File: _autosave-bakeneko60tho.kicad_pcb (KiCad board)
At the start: 2 copper layers, 285.8 x 95.2 mm, 160 parts, among them J1 Conn_01x04, SW1 SW_Push, U1 ATmega32U4-AU, Y1 16MHz

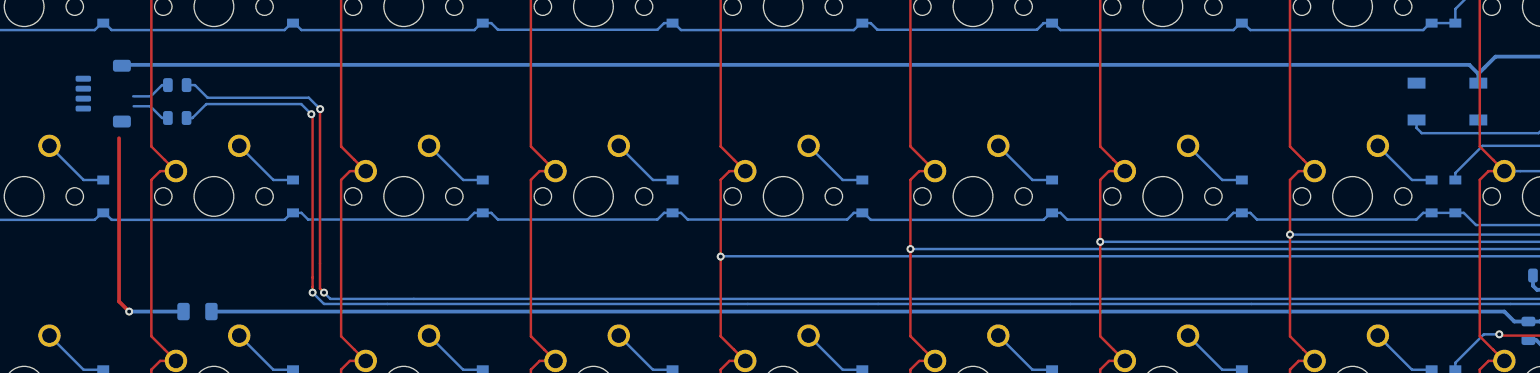
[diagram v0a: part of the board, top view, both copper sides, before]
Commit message: use jst for usb conn
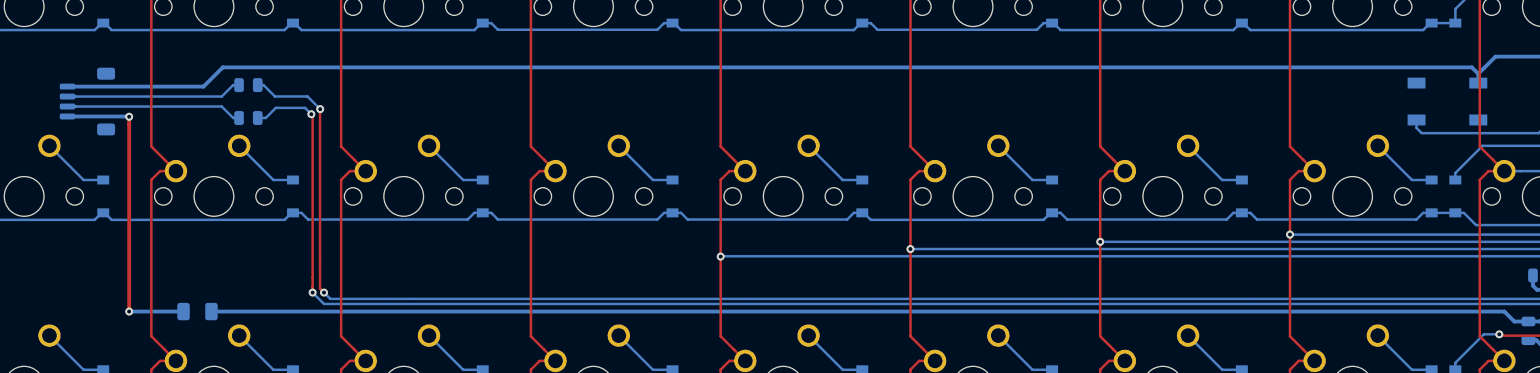
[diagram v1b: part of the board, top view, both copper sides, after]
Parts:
- moved R1 7.14 mm to (82.8, 33.4)
- moved R2 7.14 mm to (82.8, 30.1)
- moved J1 1.77 mm to (66.7, 31.8)
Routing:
- net D-: track 3.92 -> 17.7 mm
- net D+: track 3.95 -> 17.7 mm
- net VCC: track 23.3 -> 31.2 mm, vias 1 -> 2
- net Net-(R1-Pad1): track 160.2 -> 152.7 mm
- net Net-(R2-Pad1): track 160.3 -> 153.2 mm
- net GND: track 254.7 -> 260.6 mm
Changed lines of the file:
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@@
     (thickness 1.6)
     (drawings 24)
-    (tracks 1101)
+    (tracks 1107)
     (zones 0)
     (modules 160)
@@
     (visible_elements 7FFFFFFF)
     (pcbplotparams
-      (layerselection 0x010fc_ffffffff)
+      (layerselection 0x010f0_ffffffff)
       (usegerberextensions false)
       (usegerberattributes false)
@@
       (outputformat 1)
       (mirror false)
-      (drillshape 1)
+      (drillshape 0)
       (scaleselection 1)
-      (outputdirectory ""))
+      (outputdirectory "Gerbers/"))
   )
   (net 0 "")
@@
   )
   (module Connector_JST:JST_SH_SM04B-SRSS-TB_1x04-1MP_P1.00mm_Horizontal (layer B.Cu)
-    (at 68.2625 30.95625 270)
+    (at 66.675 31.75 270)
     (descr "JST SH series connector, SM04B-SRSS-TB (http://www.jst-mfg.com/product/pdf/eng/eSH.pdf), generated with kicad-footprint-generator")
     (tags "connector JST SH top entry")
@@
   )
   (module Resistor_SMD:R_0805_2012Metric (layer B.Cu)
-    (at 75.692 30.099 180)
+    (at 82.83575 30.099 180)
     (descr "Resistor SMD 0805 (2012 Metric), square (rectangular) end terminal, IPC_7351 nominal, (Body size source: https://docs.google.com/spreadsheets/d/1BsfQQcO9C6DZCsRaXUlFlo91Tg2WpOkGARC1WS5S8t0/edit?usp=sharing), generated with kicad-footprint-generator")
     (tags resistor)
@@
   )
   (module Resistor_SMD:R_0805_2012Metric (layer B.Cu)
-    (at 75.692 33.401 180)
+    (at 82.83575 33.401 180)
     (descr "Resistor SMD 0805 (2012 Metric), square (rectangular) end terminal, IPC_7351 nominal, (Body size source: https://docs.google.com/spreadsheets/d/1BsfQQcO9C6DZCsRaXUlFlo91Tg2WpOkGARC1WS5S8t0/edit?usp=sharing), generated with kicad-footprint-generator")
     (tags resistor)
@@
   (segment (start 222.8365 61.43) (end 224.13049 60.13601) (width 0.381) (layer B.Cu) (net 1))
   (segment (start 222.8365 62.23) (end 222.8365 61.43) (width 0.381) (layer B.Cu) (net 1))
-  (segment (start 205.398 28.067) (end 206.3 28.969) (width 0.381) (layer B.Cu) (net 1))
-  (segment (start 69.85 28.067) (end 205.398 28.067) (width 0.381) (layer B.Cu) (net 1))
+  (segment (start 205.652 28.321) (end 206.3 28.969) (width 0.381) (layer B.Cu) (net 1))
+  (segment (start 80.264 28.321) (end 205.652 28.321) (width 0.381) (layer B.Cu) (net 1))
+  (segment (start 64.675 30.25) (end 78.335 30.25) (width 0.381) (layer B.Cu) (net 1))
+  (segment (start 78.335 30.25) (end 80.264 28.321) (width 0.381) (layer B.Cu) (net 1))
   (segment (start 220.70725 43.0165) (end 220.70725 44.1475) (width 0.381) (layer B.Cu) (net 2))
   (segment (start 220.70725 35.139) (end 220.70725 43.0165) (width 0.381) (layer B.Cu) (net 2))
@@
   (via (at 70.866 52.832) (size 0.8) (drill 0.4) (layers F.Cu B.Cu) (net 83))
   (segment (start 70.866 52.832) (end 76.324 52.832) (width 0.381) (layer B.Cu) (net 83))
-  (segment (start 69.85 51.816) (end 70.866 52.832) (width 0.381) (layer F.Cu) (net 83))
-  (segment (start 69.85 35.433) (end 69.85 51.816) (width 0.381) (layer F.Cu) (net 83))
-  (segment (start 74.167 30.099) (end 74.7545 30.099) (width 0.25) (layer B.Cu) (net 84))
-  (segment (start 73.04 31.226) (end 74.167 30.099) (width 0.25) (layer B.Cu) (net 84))
-  (segment (start 71.271 31.226) (end 73.04 31.226) (width 0.25) (layer B.Cu) (net 84))
-  (segment (start 74.167 33.401) (end 74.7545 33.401) (width 0.25) (layer B.Cu) (net 85))
-  (segment (start 72.992 32.226) (end 74.167 33.401) (width 0.25) (layer B.Cu) (net 85))
-  (segment (start 71.319 32.226) (end 72.992 32.226) (width 0.25) (layer B.Cu) (net 85))
+  (segment (start 64.675 33.25) (end 70.588 33.25) (width 0.381) (layer B.Cu) (net 83))
+  (segment (start 70.866 34.093685) (end 70.866 52.832) (width 0.381) (layer F.Cu) (net 83))
+  (via (at 70.866 33.274) (size 0.8) (drill 0.4) (layers F.Cu B.Cu) (net 83))
+  (segment (start 70.588 33.25) (end 70.842 33.25) (width 0.381) (layer B.Cu) (net 83))
+  (segment (start 70.842 33.25) (end 70.866 33.274) (width 0.381) (layer B.Cu) (net 83))
+  (segment (start 70.866 33.274) (end 70.866 34.093685) (width 0.381) (layer F.Cu) (net 83))
+  (segment (start 65.55 31.25) (end 64.675 31.25) (width 0.25) (layer B.Cu) (net 84))
+  (segment (start 80.15975 31.25) (end 65.55 31.25) (width 0.25) (layer B.Cu) (net 84))
+  (segment (start 81.31075 30.099) (end 80.15975 31.25) (width 0.25) (layer B.Cu) (net 84))
+  (segment (start 81.89825 30.099) (end 81.31075 30.099) (width 0.25) (layer B.Cu) (net 84))
+  (segment (start 65.55 32.25) (end 64.675 32.25) (width 0.25) (layer B.Cu) (net 85))
+  (segment (start 80.15975 32.25) (end 65.55 32.25) (width 0.25) (layer B.Cu) (net 85))
+  (segment (start 81.31075 33.401) (end 80.15975 32.25) (width 0.25) (layer B.Cu) (net 85))
+  (segment (start 81.89825 33.401) (end 81.31075 33.401) (width 0.25) (layer B.Cu) (net 85))
   (segment (start 17.290001 37.610001) (end 18.415 38.735) (width 0.25) (layer F.Cu) (net 86))
   (segment (start 15.944999 36.264999) (end 17.290001 37.610001) (width 0.25) (layer F.Cu) (net 86))
@@
   (segment (start 89.281 49.403) (end 89.281 33.147) (width 0.25) (layer F.Cu) (net 101))
   (segment (start 89.281 33.147) (end 89.154 33.02) (width 0.25) (layer F.Cu) (net 101))
-  (segment (start 77.217 33.401) (end 76.6295 33.401) (width 0.25) (layer B.Cu) (net 101))
-  (segment (start 77.217 33.4) (end 77.217 33.401) (width 0.25) (layer B.Cu) (net 101))
-  (segment (start 78.613 32.004) (end 77.217 33.4) (width 0.25) (layer B.Cu) (net 101))
-  (segment (start 89.154 33.02) (end 88.138 32.004) (width 0.25) (layer B.Cu) (net 101))
-  (segment (start 88.138 32.004) (end 78.613 32.004) (width 0.25) (layer B.Cu) (net 101))
-  (segment (start 216.2685 51.4475) (end 216.154 51.562) (width 0.25) (layer B.Cu) (net 102))
-  (segment (start 217.40725 51.4475) (end 216.2685 51.4475) (width 0.25) (layer B.Cu) (net 102))
-  (segment (start 99.441 51.562) (end 91.059 51.562) (width 0.25) (layer B.Cu) (net 102))
-  (segment (start 91.059 51.562) (end 90.424 50.927) (width 0.25) (layer B.Cu) (net 102))
-  (segment (start 216.154 51.562) (end 99.441 51.562) (width 0.25) (layer B.Cu) (net 102))
+  (segment (start 83.77325 33.401) (end 84.582 33.401) (width 0.25) (layer B.Cu) (net 101))
+  (segment (start 84.582 33.401) (end 85.598 32.385) (width 0.25) (layer B.Cu) (net 101))
+  (segment (start 88.519 32.385) (end 89.154 33.02) (width 0.25) (layer B.Cu) (net 101))
+  (segment (start 85.598 32.385) (end 88.519 32.385) (width 0.25) (layer B.Cu) (net 101))
   (via (at 90.424 50.927) (size 0.8) (drill 0.4) (layers F.Cu B.Cu) (net 102))
-  (segment (start 90.024001 50.527001) (end 90.024001 48.024999) (width 0.25) (layer F.Cu) (net 102))
-  (segment (start 90.424 50.927) (end 90.024001 50.527001) (width 0.25) (layer F.Cu) (net 102))
   (via (at 90.043 32.512) (size 0.8) (drill 0.4) (layers F.Cu B.Cu) (net 102))
   (segment (start 90.024001 48.024999) (end 90.024001 32.530999) (width 0.25) (layer F.Cu) (net 102))
+  (segment (start 90.024001 50.527001) (end 90.024001 48.024999) (width 0.25) (layer F.Cu) (net 102))
+  (segment (start 217.40725 51.4475) (end 216.2685 51.4475) (width 0.25) (layer B.Cu) (net 102))
+  (segment (start 90.424 50.927) (end 90.024001 50.527001) (width 0.25) (layer F.Cu) (net 102))
+  (segment (start 91.059 51.562) (end 90.424 50.927) (width 0.25) (layer B.Cu) (net 102))
+  (segment (start 99.441 51.562) (end 91.059 51.562) (width 0.25) (layer B.Cu) (net 102))
   (segment (start 90.024001 32.530999) (end 90.043 32.512) (width 0.25) (layer F.Cu) (net 102))
-  (segment (start 89.643001 32.112001) (end 90.043 32.512) (width 0.25) (layer B.Cu) (net 102))
-  (segment (start 88.9 31.369) (end 89.643001 32.112001) (width 0.25) (layer B.Cu) (net 102))
-  (segment (start 78.74 31.369) (end 88.9 31.369) (width 0.25) (layer B.Cu) (net 102))
-  (segment (start 76.6295 30.099) (end 77.47 30.099) (width 0.25) (layer B.Cu) (net 102))
-  (segment (start 77.47 30.099) (end 78.74 31.369) (width 0.25) (layer B.Cu) (net 102))
+  (segment (start 216.2685 51.4475) (end 216.154 51.562) (width 0.25) (layer B.Cu) (net 102))
+  (segment (start 216.154 51.562) (end 99.441 51.562) (width 0.25) (layer B.Cu) (net 102))
+  (segment (start 84.36075 30.099) (end 85.50375 31.242) (width 0.25) (layer B.Cu) (net 102))
+  (segment (start 83.77325 30.099) (end 84.36075 30.099) (width 0.25) (layer B.Cu) (net 102))
+  (segment (start 88.773 31.242) (end 90.043 32.512) (width 0.25) (layer B.Cu) (net 102))
+  (segment (start 85.50375 31.242) (end 88.773 31.242) (width 0.25) (layer B.Cu) (net 102))
   (segment (start 200.1 34.4) (end 200.625 34.925) (width 0.25) (layer B.Cu) (net 103))
   (segment (start 200.1 33.6) (end 200.1 34.4) (width 0.25) (layer B.Cu) (net 103))
